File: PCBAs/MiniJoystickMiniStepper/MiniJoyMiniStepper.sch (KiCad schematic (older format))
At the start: 21 parts, among them J1 STEPPER_UNI_5P, J10 TH_0.1_1x1, J11 TH_0.1_1x1, J2 STEPPER_UNI_5P, J28 TH_0.1_1x1, J29 TH_0.1_1x1, J50 STEPPER_UNI_5P, J51 STEPPER_UNI_5P, J6 TH_0.1_1x1, J7 TH_0.1_1x1, J8 TH_0.1_1x1, J9 TH_0.1_1x1, U1 ADAFRUIT_FEATHER_M0, U2 ULN2803, U3 ULN2803

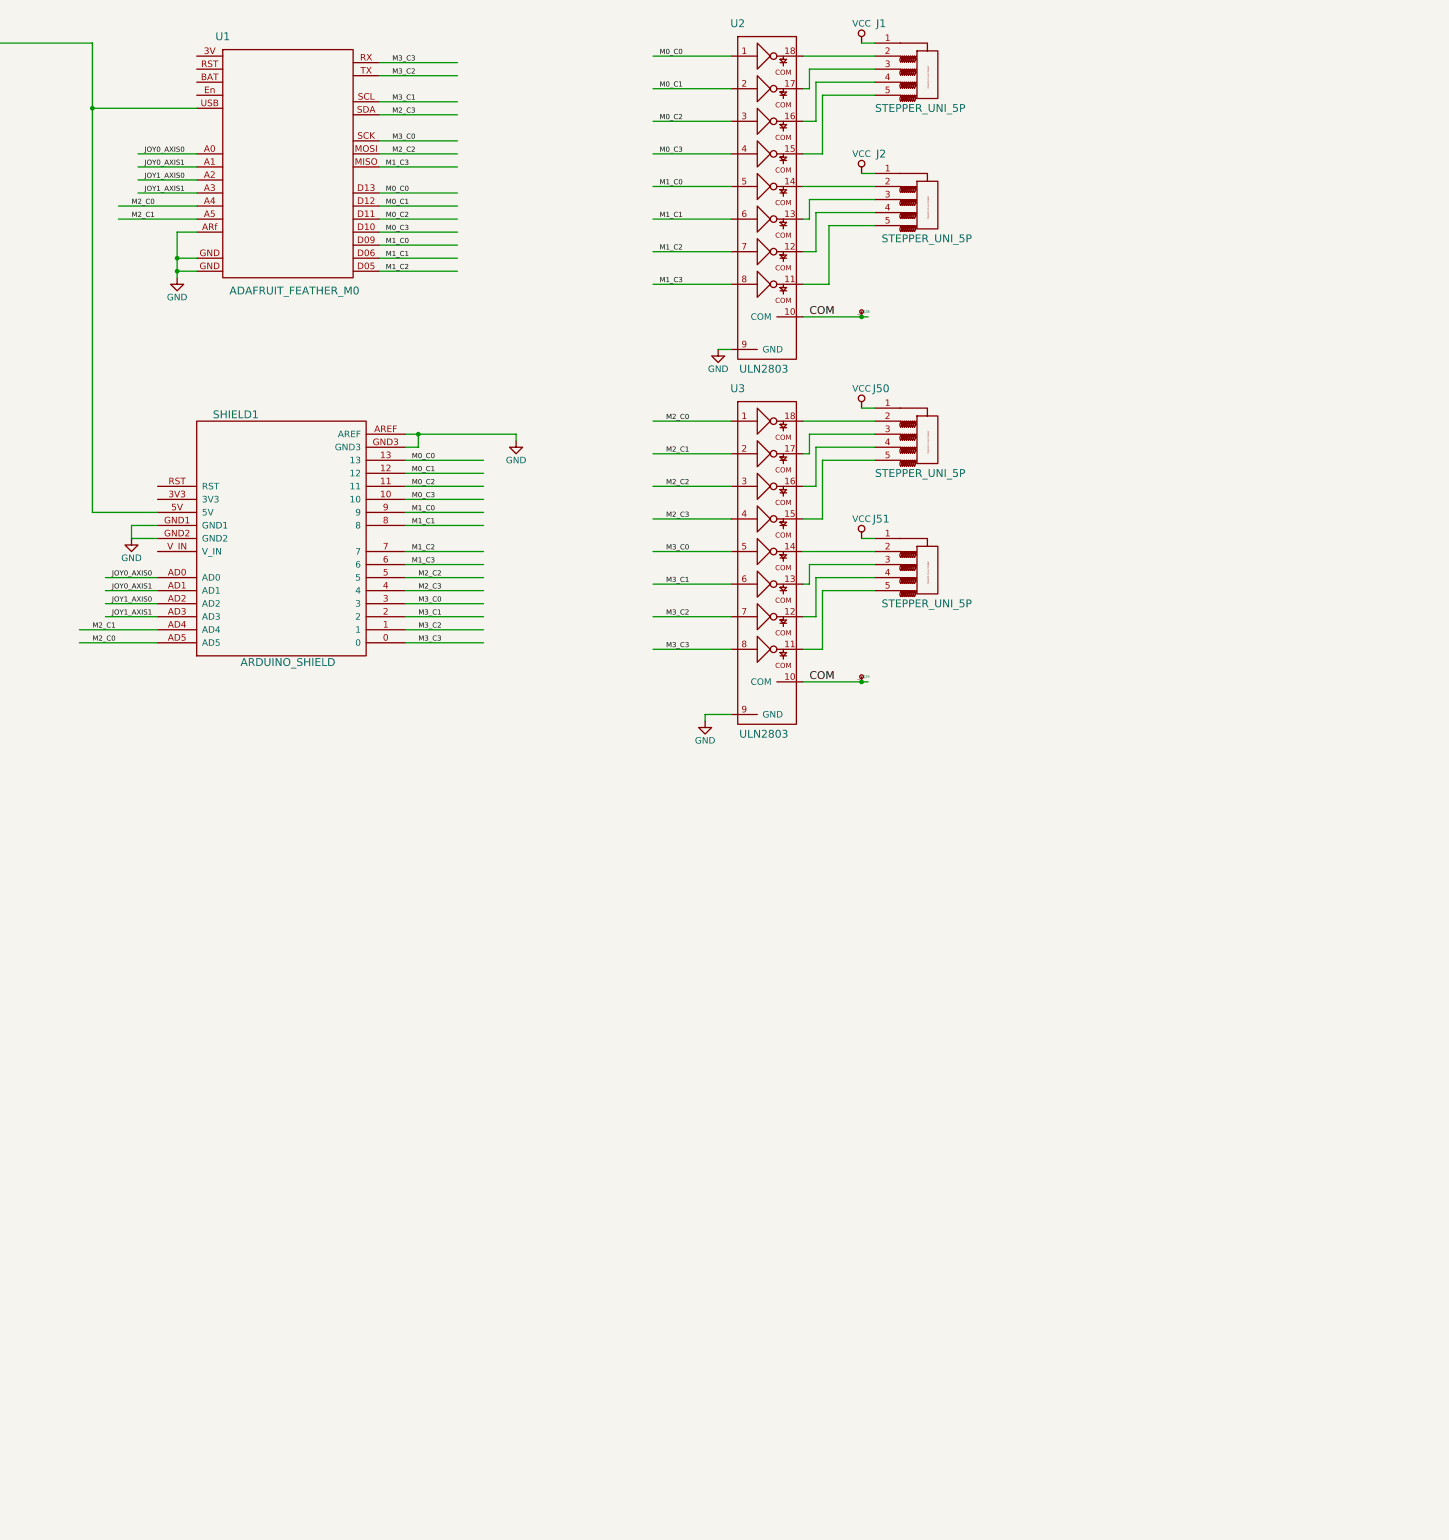
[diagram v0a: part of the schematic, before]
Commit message: Added shift register to library
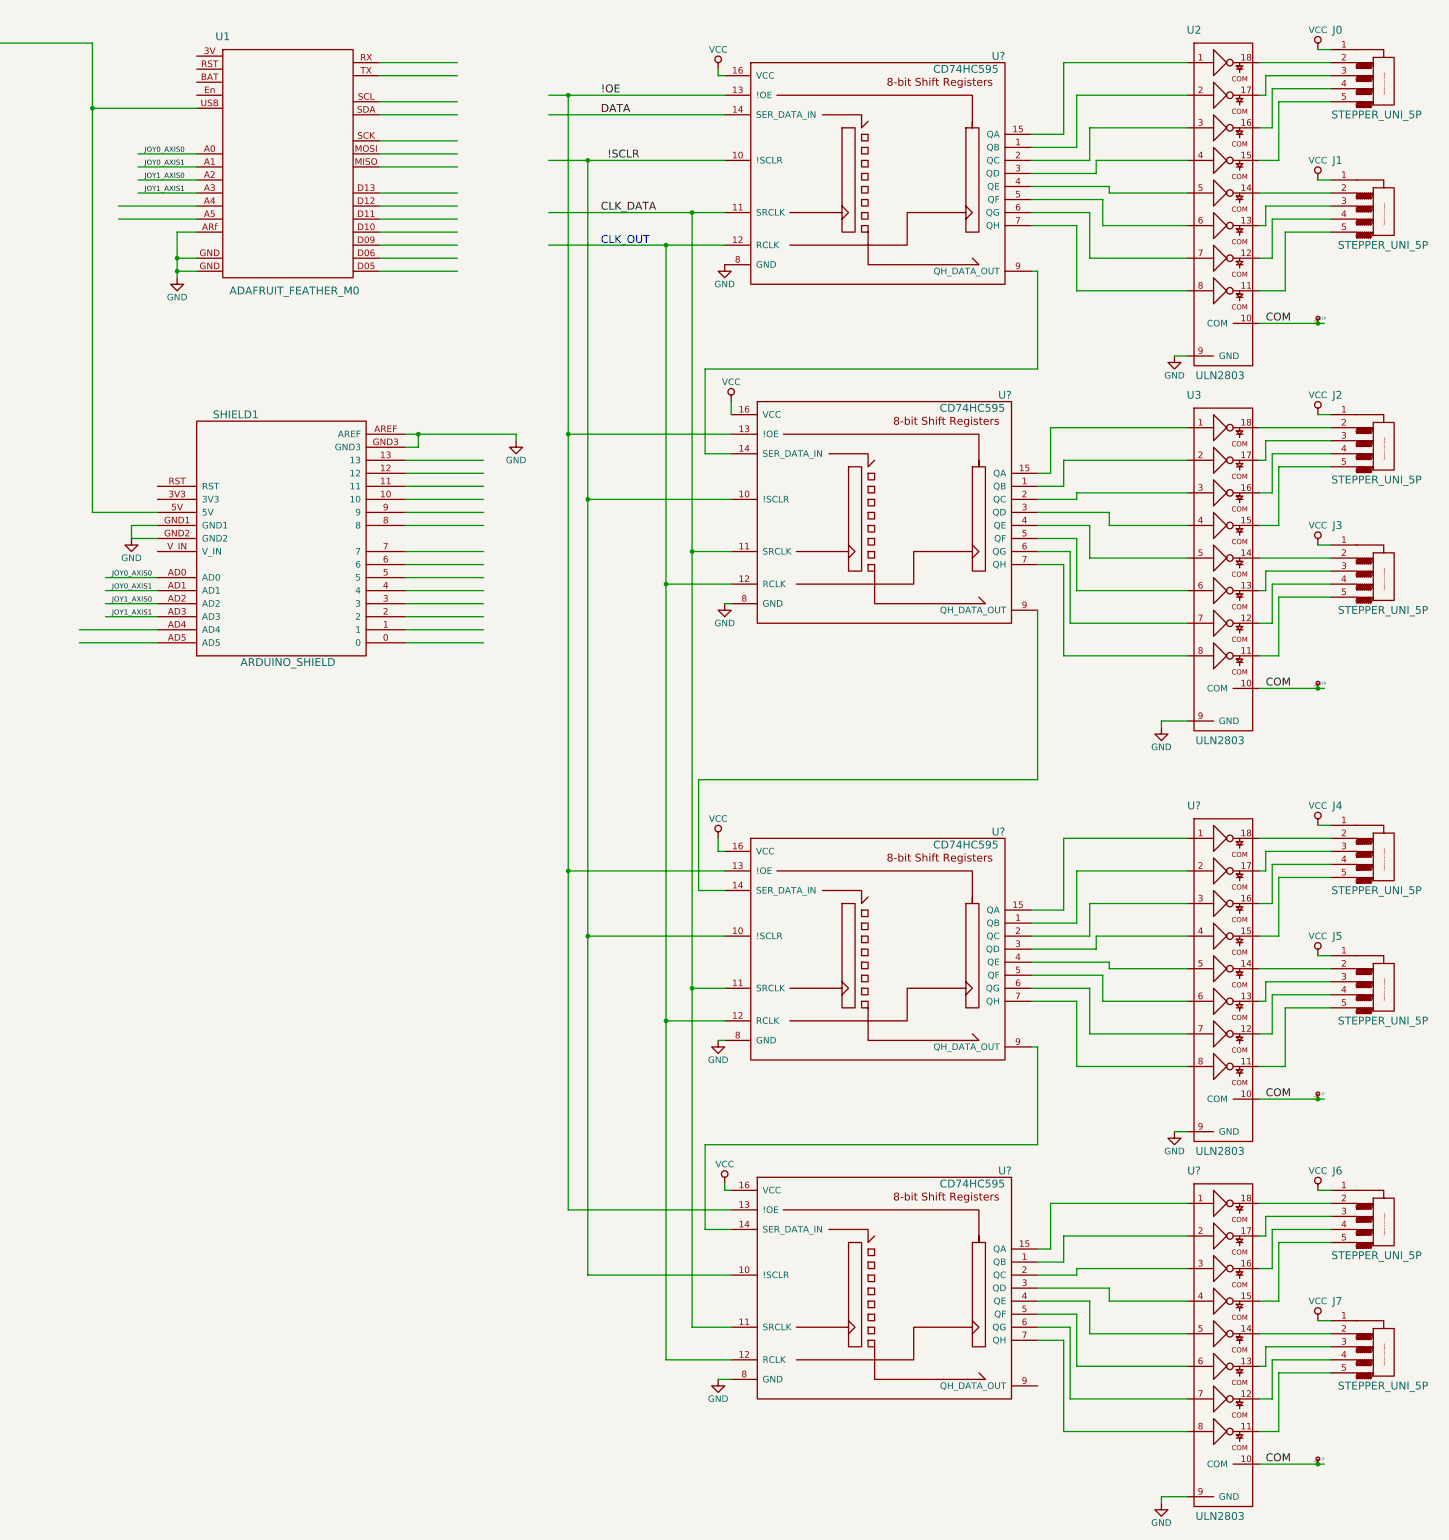
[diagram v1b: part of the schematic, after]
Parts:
- added J4, J5, J6, J7: STEPPER_UNI_5P, Liberry:M20-1060500_DEBUG, symbol STEPPER_UNI_5P
- added J? (x2): TH_0.1_1x1, Liberry:single_0.1, symbol TH_0.1_1x1
- added U? (x4): CD74HC595, MiniJoystickMiniStepper:SOIC-16_1.27x9.3, symbol CD74HC595
- added U? (x2): ULN2803, symbol ULN2803
- renumbered J1 to J0, J2 to J1, J50 to J2, J51 to J3
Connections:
- net labels added: !OE, !SCLR, CLK_DATA, DATA
- net labels removed: M0_C0, M0_C1, M0_C2, M0_C3, M1_C0, M1_C1, M1_C2, M1_C3, M2_C0, M2_C1, M2_C2, M2_C3, M3_C0, M3_C1, M3_C2, M3_C3
- wire segments 146 -> 320
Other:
- note added: "CLK_OUT\n"
- moved on the sheet: J0, J1, J2, J28, J29, J3, U2, U3

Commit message: Added ARM M0, Osc, Joystick, and other footprints/symbols
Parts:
- removed SHIELD1: ARDUINO_SHIELD, Liberry:ARDUINO_SHIELD_2_debug, symbol ARDUINO_SHIELD
- added J11, J12, J13, J14, J15, J16: TH_0.1_1x1, Liberry:single_0.1, symbol TH_0.1_1x1
- added R2, R3: XYJOY, MiniJoystickMiniStepper:JOY_ALPS_RKJXV1224005, symbol XYJOY
- added U1: ATSAMD21G18A, MiniJoystickMiniStepper:QFP_48_0.5_8, symbol ATSAMD21G18A
- added U2: OLED_128x32_I2C, MiniJoystickMiniStepper:OLED_128x32, symbol OLED_128x32_I2C
- added V_3.3, V_USB1: CONN_01X01, Liberry:TH_0.1_1x2_Jumper, symbol CONN_01X01
- added X1: SIT1533_MEMS_OSC, MiniJoystickMiniStepper:SiTime1533, symbol SIT1533_MEMS_OSC
- R0: renamed from R1; footprint Liberry:XY_JOY_254TA103B50B -> MiniJoystickMiniStepper:JOY_ALPS_RKJXV1224005
- R1: renamed from R2; footprint Liberry:XY_JOY_254TA103B50B -> MiniJoystickMiniStepper:JOY_ALPS_RKJXV1224005
- U10, U9: renamed from U?; footprint (none) -> MiniJoystickMiniStepper:SOIC-18_1.27_9.4
- U7: renamed from U2; footprint (none) -> MiniJoystickMiniStepper:SOIC-18_1.27_9.4
- U8: renamed from U3; footprint (none) -> MiniJoystickMiniStepper:SOIC-18_1.27_9.4
- gave numbers to parts that had none: 6
- renumbered COM0 to COM1, J28 to J100, J10 to J101, J9 to J102, J8 to J103, J7 to J104, J6 to J105, J11 to J107, J29 to J8, U1 to JF1000, VCC1 to V_MOTOR1
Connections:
- net labels added: JOY2_AXIS0, JOY2_AXIS1, JOY2_SW, JOY3_AXIS0, JOY3_AXIS1, JOY3_SW, MOTOR_POWER, V_USB
- wire segments 320 -> 344

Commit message: Finished first pass schematic
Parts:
- removed JF1000: ADAFRUIT_FEATHER_M0, Liberry:ADAFRUIT_FEATHER_debug_1, symbol ADAFRUIT_FEATHER_M0
- removed U1: ATSAMD21G18A, MiniJoystickMiniStepper:QFP_48_0.5_8, symbol ATSAMD21G18A
- removed X1: SIT1533_MEMS_OSC, MiniJoystickMiniStepper:SiTime1533, symbol SIT1533_MEMS_OSC
- added C1: 0.1 uF, Capacitors_SMD:C_0603, symbol C
- added J_+3.3V1, J_CAN_RX1, J_CAN_TX1, J_GND1, J_UART1_RX1, J_UART1_TX1: TH_0.1_1x1, Liberry:single_0.1, symbol TH_0.1_1x1
- added R101, R102: 10K, Resistors_SMD:R_0603, symbol R
- added R99: 0, Resistors_SMD:R_0603, symbol R
- added U1: MCP3008T-I/SL, symbol MCP3008T-I/SL
- added U11: STM32F103C8T6_BLUE_PILL, symbol STM32F103C8T6_BLUE_PILL
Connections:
- net labels added: !MOTOR_OE, !MOTOR_SCLR, +3.3V, +5V, I2C1_SCL, I2C1_SDA, MOTOR_CLK_DATA, MOTOR_CLK_OUT, MOTOR_DATA, SPI1_CS, SPI1_MISO, SPI1_MOSI, SPI1_SCK
- net labels removed: !OE, !SCLR, CLK_DATA, DATA
- wire segments 344 -> 391
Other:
- note removed: "CLK_OUT\n"
- moved on the sheet: COM1, GND1, J0, J1, J10, J100, J101, J102, J103, J104, J105, J107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

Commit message: Added missing footprints to sch
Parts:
- U1: footprint (none) -> MiniJoystickMiniStepper:SOIC-16
- U11: footprint (none) -> MiniJoystickMiniStepper:BLUEPILL_CORTEXM3_STM32F103C8T6
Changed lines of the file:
@@
 F 0 "U11" H 11650 8400 60  0000 C CNN
 F 1 "STM32F103C8T6_BLUE_PILL" H 10800 8300 60  0000 C CNN
-F 2 "" H 10850 7200 60  0001 C CNN
+F 2 "MiniJoystickMiniStepper:BLUEPILL_CORTEXM3_STM32F103C8T6" H 10850 7200 60  0001 C CNN
 F 3 "" H 10850 7200 60  0001 C CNN
 	1    10850 7200
@@
 F 0 "U1" H 5450 4950 60  0000 C CNN
 F 1 "MCP3008T-I/SL" H 5450 3100 60  0000 C CNN
-F 2 "" H 5450 4050 60  0001 C CNN
+F 2 "MiniJoystickMiniStepper:SOIC-16" H 5450 4050 60  0001 C CNN
 F 3 "" H 5450 4050 60  0001 C CNN
 	1    5450 4050
